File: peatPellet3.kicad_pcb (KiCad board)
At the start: 2 copper layers, 87.6 x 55.9 mm, 63 parts, among them J1 Barrel_Jack_Switch, J2 AudioJack2, J3 AudioJack2, K1 Relay_DPDT, SW1 SW_SPDT, SW2 SW_SPDT, SW3 SW_SPDT_MSM, U1 TL072, U2 L78L05_SO8, U3 LM555xM

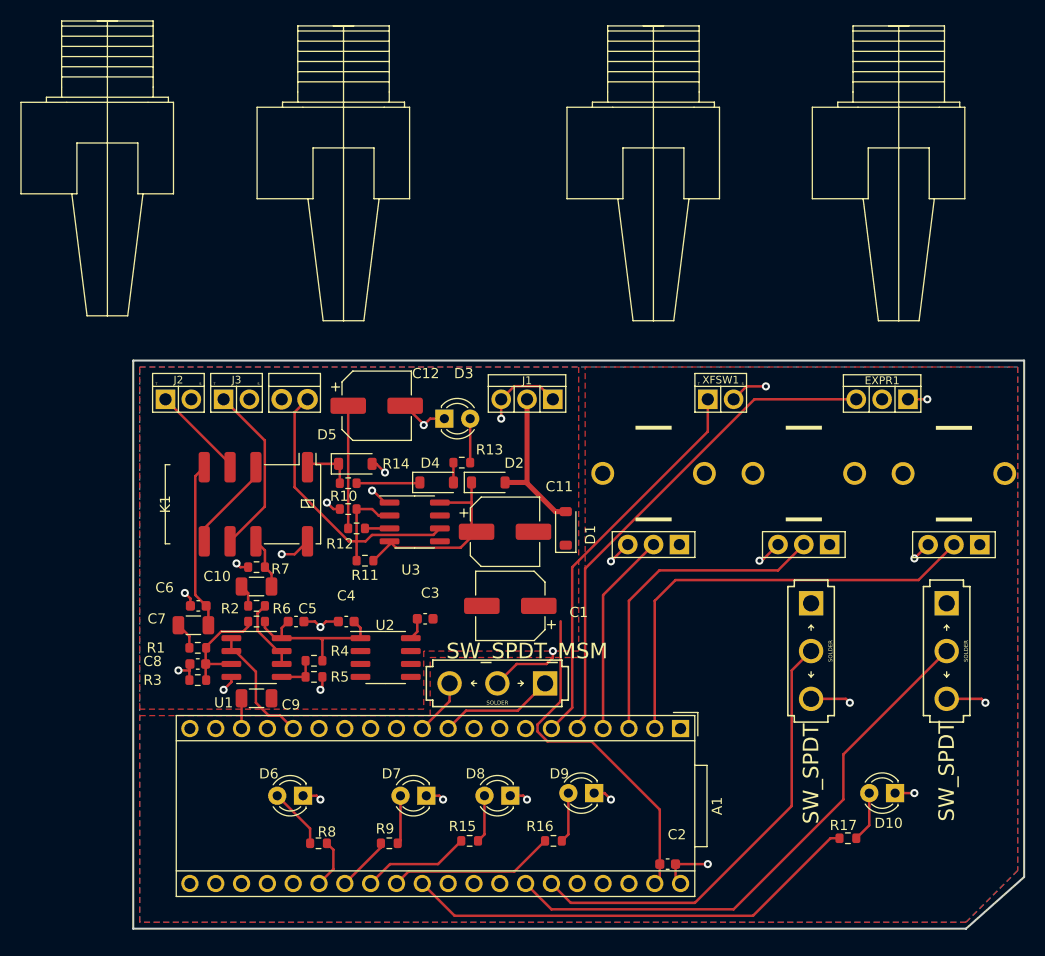
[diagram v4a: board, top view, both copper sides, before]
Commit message: power updates: grounding, 3.3v pour
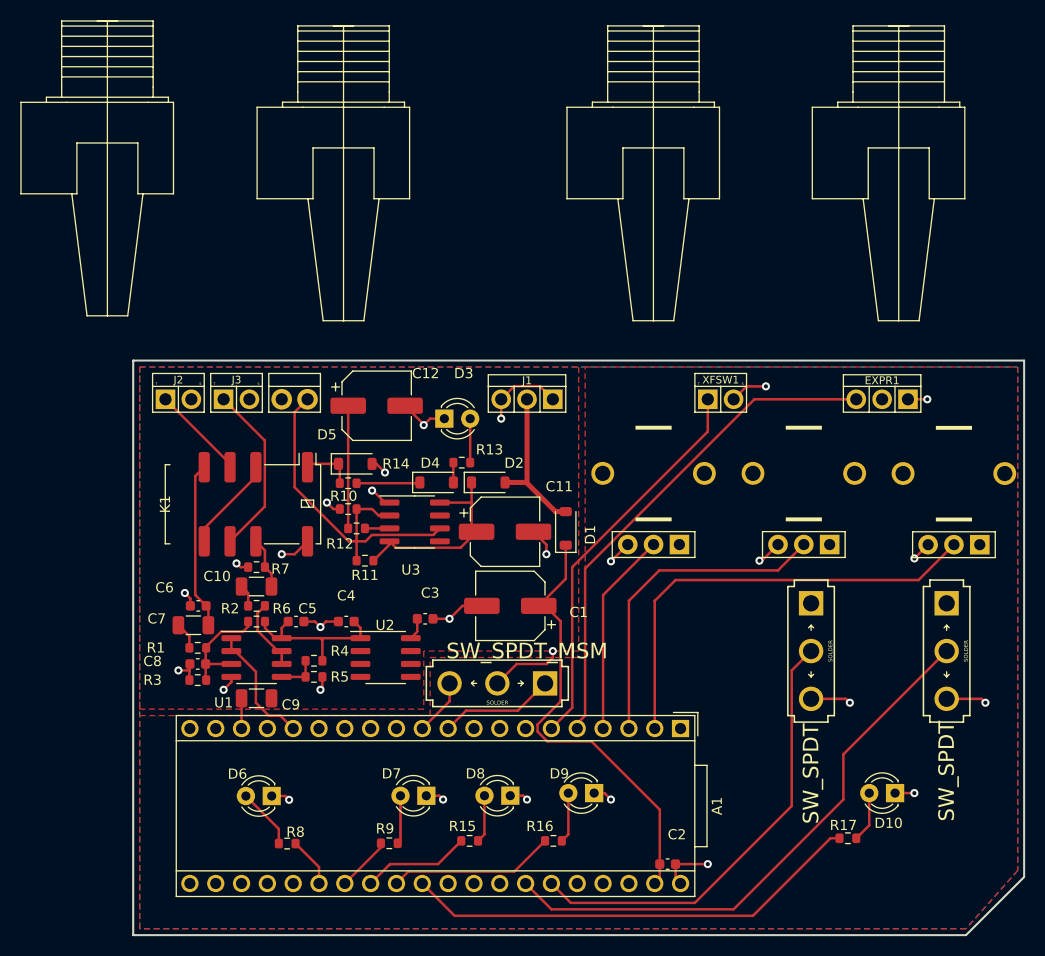
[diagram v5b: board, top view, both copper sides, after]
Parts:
- moved R8 3.08 mm to (97.7, 133.9)
- moved D6 3.08 mm to (96.2, 129.2)
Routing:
- net +9V: track 56.8 -> 66.7 mm
- net GND: track 75.8 -> 83.9 mm, vias 26 -> 28
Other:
- board size 87.6 x 55.9 mm -> 87.6 x 56.5 mm
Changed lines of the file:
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@@
   (net 68 "unconnected-(A1-ADC_3-Pad25)")
   (footprint "Resistor_SMD:R_0603_1608Metric" (layer "F.Cu")
-    (at 100.775 133.839972 180)
+    (at 97.6925 133.8675 180)
     (descr "Resistor SMD 0603 (1608 Metric), square (rectangular) end terminal, IPC_7351 nominal, (Body size source: IPC-SM-782 page 72, https://www.pcb-3d.com/wordpress/wp-content/uploads/ipc-sm-782a_amendment_1_and_2.pdf), generated with kicad-footprint-generator")
     (tags "resistor")
@@
   )
   (footprint "LED_THT:LED_D3.0mm" (layer "F.Cu")
-    (at 99.255 129.164972 180)
+    (at 96.1725 129.1925 180)
     (descr "LED, diameter 3.0mm, 2 pins")
     (tags "LED diameter 3.0mm 2 pins")
@@
     (pts
       (xy 82.55 86.36)
-      (xy 82.55 142.24)
-      (xy 164.465 142.24)
+      (xy 82.55 142.875)
+      (xy 164.465 142.875)
       (xy 170.18 137.16)
       (xy 170.18 86.36)
@@
   (segment (start 98.425 105.41) (end 97.155 105.41) (width 0.25) (layer "F.Cu") (net 17))
   (segment (start 93.075 106.68) (end 92.71 106.315) (width 0.25) (layer "F.Cu") (net 17))
+  (segment (start 114.935 110.49) (end 113.665 111.76) (width 0.25) (layer "F.Cu") (net 17))
   (segment (start 165.989 119.634) (end 166.37 120.015) (width 0.25) (layer "F.Cu") (net 17))
   (segment (start 157.485 128.905) (end 159.385 128.905) (width 0.25) (layer "F.Cu") (net 17))
   (segment (start 119.639 129.16) (end 120.904 129.16) (width 0.25) (layer "F.Cu") (net 17))
   (segment (start 101.155 118.555) (end 100.965 118.745) (width 0.25) (layer "F.Cu") (net 17))
-  (segment (start 100.589972 129.164972) (end 100.965 129.54) (width 0.25) (layer "F.Cu") (net 17))
+  (segment (start 97.507472 129.1925) (end 97.8825 129.567528) (width 0.25) (layer "F.Cu") (net 17))
   (segment (start 123.825 115.57) (end 123.825 114.935) (width 0.25) (layer "F.Cu") (net 17))
   (segment (start 111.76 92.075) (end 111.125 92.71) (width 0.25) (layer "F.Cu") (net 17))
@@
   (segment (start 135.89 137.3) (end 136.385 137.795) (width 0.25) (layer "F.Cu") (net 17))
   (segment (start 120.269 116.205) (end 123.19 116.205) (width 0.25) (layer "F.Cu") (net 17))
-  (segment (start 99.255 129.164972) (end 100.589972 129.164972) (width 0.25) (layer "F.Cu") (net 17))
+  (segment (start 96.1725 129.1925) (end 97.507472 129.1925) (width 0.25) (layer "F.Cu") (net 17))
   (segment (start 109.295 90.805) (end 111.125 92.635) (width 0.25) (layer "F.Cu") (net 17))
   (segment (start 88.175 109.765) (end 87.63 109.22) (width 0.25) (layer "F.Cu") (net 17))
+  (segment (start 121.92 103.2) (end 123.19 104.47) (width 0.25) (layer "F.Cu") (net 17))
   (segment (start 88.075 116.84) (end 88.075 116.255) (width 0.25) (layer "F.Cu") (net 17))
   (segment (start 99.695 104.14) (end 98.425 105.41) (width 0.25) (layer "F.Cu") (net 17))
@@
   (segment (start 111.379 129.164972) (end 112.653972 129.164972) (width 0.25) (layer "F.Cu") (net 17))
   (segment (start 129.54 106.1085) (end 131.191 104.4575) (width 0.25) (layer "F.Cu") (net 17))
+  (segment (start 123.19 104.47) (end 123.19 105.41) (width 0.25) (layer "F.Cu") (net 17))
   (segment (start 144.145 106.045) (end 144.3825 106.045) (width 0.25) (layer "F.Cu") (net 17))
   (segment (start 120.0352 88.8798) (end 122.5348 88.8798) (width 0.25) (layer "F.Cu") (net 17))
   (segment (start 127.889 128.905) (end 128.904 128.905) (width 0.25) (layer "F.Cu") (net 17))
+  (segment (start 116.84 110.49) (end 114.935 110.49) (width 0.25) (layer "F.Cu") (net 17))
   (segment (start 128.904 128.905) (end 129.539 129.54) (width 0.25) (layer "F.Cu") (net 17))
   (segment (start 100.4195 112.03) (end 100.965 112.5755) (width 0.25) (layer "F.Cu") (net 17))
@@
   (segment (start 141.605 90.17) (end 142.875 88.9) (width 0.25) (layer "F.Cu") (net 17))
   (segment (start 111.125 92.635) (end 111.125 92.71) (width 0.25) (layer "F.Cu") (net 17))
+  (segment (start 112.04 111.76) (end 113.665 111.76) (width 0.25) (layer "F.Cu") (net 17))
   (segment (start 99.34 112.03) (end 100.4195 112.03) (width 0.25) (layer "F.Cu") (net 17))
   (segment (start 149.225 119.634) (end 152.654 119.634) (width 0.25) (layer "F.Cu") (net 17))
@@
   (via (at 160.655 90.17) (size 0.8) (drill 0.4) (layers "F.Cu" "B.Cu") (net 17))
   (via (at 100.965 112.5755) (size 0.8) (drill 0.4) (layers "F.Cu" "B.Cu") (net 17))
-  (via (at 100.965 129.54) (size 0.8) (drill 0.4) (layers "F.Cu" "B.Cu") (net 17))
+  (via (at 97.8825 129.567528) (size 0.8) (drill 0.4) (layers "F.Cu" "B.Cu") (net 17))
   (via (at 106.045 99.1495) (size 0.8) (drill 0.4) (layers "F.Cu" "B.Cu") (net 17))
   (via (at 92.71 106.315) (size 0.8) (drill 0.4) (layers "F.Cu" "B.Cu") (net 17))
   (via (at 144.145 106.045) (size 0.8) (drill 0.4) (layers "F.Cu" "B.Cu") (net 17))
   (via (at 129.539 129.54) (size 0.8) (drill 0.4) (layers "F.Cu" "B.Cu") (net 17))
+  (via (at 123.19 105.41) (size 0.8) (drill 0.4) (layers "F.Cu" "B.Cu") (net 17))
   (via (at 97.155 105.41) (size 0.8) (drill 0.4) (layers "F.Cu" "B.Cu") (net 17))
   (via (at 111.125 92.71) (size 0.8) (drill 0.4) (layers "F.Cu" "B.Cu") (net 17))
@@
   (via (at 159.385 128.905) (size 0.8) (drill 0.4) (layers "F.Cu" "B.Cu") (net 17))
   (via (at 153.035 120.015) (size 0.8) (drill 0.4) (layers "F.Cu" "B.Cu") (net 17))
+  (via (at 113.665 111.76) (size 0.8) (drill 0.4) (layers "F.Cu" "B.Cu") (net 17))
   (via (at 129.54 106.1085) (size 0.8) (drill 0.4) (layers "F.Cu" "B.Cu") (net 17))
   (via (at 166.37 120.015) (size 0.8) (drill 0.4) (layers "F.Cu" "B.Cu") (net 17))
@@
   (segment (start 143.653881 90.17) (end 153.67 90.17) (width 0.25) (layer "F.Cu") (net 22))
   (segment (start 127 106.823881) (end 143.653881 90.17) (width 0.25) (layer "F.Cu") (net 22))
-  (segment (start 102.235 134.474972) (end 102.235 136.385) (width 0.25) (layer "F.Cu") (net 23))
-  (segment (start 102.235 136.385) (end 100.825 137.795) (width 0.25) (layer "F.Cu") (net 23))
-  (segment (start 101.6 133.839972) (end 102.235 134.474972) (width 0.25) (layer "F.Cu") (net 23))
+  (segment (start 100.825 136.175) (end 98.5175 133.8675) (width 0.25) (layer "F.Cu") (net 23))
+  (segment (start 100.825 137.795) (end 100.825 136.175) (width 0.25) (layer "F.Cu") (net 23))
   (segment (start 106.914 133.839972) (end 106.914 134.246) (width 0.25) (layer "F.Cu") (net 24))
   (segment (start 106.914 134.246) (end 103.365 137.795) (width 0.25) (layer "F.Cu") (net 24))
@@
   (segment (start 103.695 102.87) (end 103.695 90.805) (width 0.25) (layer "F.Cu") (net 54))
   (segment (start 115.695 92.075) (end 115.695 96.52) (width 0.25) (layer "F.Cu") (net 55))
-  (segment (start 99.95 132.399972) (end 99.95 133.839972) (width 0.25) (layer "F.Cu") (net 56))
-  (segment (start 96.715 129.164972) (end 99.95 132.399972) (width 0.25) (layer "F.Cu") (net 56))
+  (segment (start 96.8675 132.4275) (end 96.8675 133.8675) (width 0.25) (layer "F.Cu") (net 56))
+  (segment (start 93.6325 129.1925) (end 96.8675 132.4275) (width 0.25) (layer "F.Cu") (net 56))
   (segment (start 108.839 133.564972) (end 108.564 133.839972) (width 0.25) (layer "F.Cu") (net 57))
   (segment (start 108.839 129.164972) (end 108.839 133.564972) (width 0.25) (layer "F.Cu") (net 57))
@@
   (segment (start 107.76 104.455) (end 107.76 104.14) (width 0.25) (layer "F.Cu") (net 66))
   (segment (start 112.71 100.33) (end 115.825 100.33) (width 0.25) (layer "F.Cu") (net 66))
+  (segment (start 125.095 104.52) (end 125.095 107.835) (width 0.25) (layer "F.Cu") (net 66))
   (segment (start 124.588 119.887) (end 122.32 122.155) (width 0.25) (layer "F.Cu") (net 66))
   (segment (start 110.49 113.03) (end 109.855 113.665) (width 0.25) (layer "F.Cu") (net 66))
+  (segment (start 122.44 110.49) (end 123.075 110.49) (width 0.25) (layer "F.Cu") (net 66))
   (segment (start 108.385 104.765) (end 114.755 104.765) (width 0.25) (layer "F.Cu") (net 66))
   (segment (start 134.34 130.53) (end 127.635 123.825) (width 0.25) (layer "F.Cu") (net 66))
@@
   (segment (start 115.825 98.35) (end 115.825 100.33) (width 0.25) (layer "F.Cu") (net 66))
   (segment (start 110.49 111.76) (end 110.49 113.03) (width 0.25) (layer "F.Cu") (net 66))
+  (segment (start 125.095 107.835) (end 122.44 110.49) (width 0.25) (layer "F.Cu") (net 66))
   (segment (start 115.825 102.705) (end 116.32 103.2) (width 0.25) (layer "F.Cu") (net 66))
   (segment (start 115.825 100.33) (end 115.825 102.705) (width 0.25) (layer "F.Cu") (net 66))
@@
   (segment (start 123.293299 123.825) (end 127.635 123.825) (width 0.25) (layer "F.Cu") (net 66))
   (segment (start 134.34 135.89) (end 134.34 137.3) (width 0.25) (layer "F.Cu") (net 66))
+  (segment (start 123.075 110.49) (end 124.588 112.003) (width 0.25) (layer "F.Cu") (net 66))
   (zone (net 66) (net_name "+9V") (layer "F.Cu") (hatch edge 0.5)
     (priority 1)
@@
         (xy 169.545 86.995)
         (xy 169.545 136.525)
-        (xy 164.465 141.605)
-        (xy 83.185 141.605)
+        (xy 164.465 142.24)
+        (xy 83.185 142.24)
         (xy 83.185 121.285)
         (xy 111.76 121.285)
@@
         (xy 169.545 86.995)
         (xy 169.545 136.525)
-        (xy 164.465 141.605)
-        (xy 83.185 141.605)
+        (xy 164.465 142.24)
+        (xy 83.185 142.24)
       )
     )

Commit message: via updates
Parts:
- D10, D6, D7, D8, D9: moved to B.Cu
- moved D9 3.06 mm to (124.8, 129.2), turned to 0 degrees
- moved D8 2.80 mm to (116.8, 129.2), turned to 0 degrees
- moved D10 2.55 mm to (154.9, 128.9), turned to 0 degrees
- moved D7 2.54 mm to (108.8, 129.2), turned to 0 degrees
- moved D6 1.85 mm to (94.3, 129.2), turned to 0 degrees
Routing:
- net GND: track 83.9 -> 50.1 mm, vias 28 -> 12
- net Net-(U1B-+): track 3.94 -> 6.46 mm
- net Net-(D10-A): track 4.97 -> 6.39 mm
- net Net-(D6-A): track 6.01 -> 4.70 mm
- net Net-(D7-A): track 4.79 -> 5.84 mm
- net Net-(D8-A): track 4.71 -> 5.72 mm
- net Net-(D9-A): track 4.97 -> 5.63 mm

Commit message: LED flips
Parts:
- D3: moved to B.Cu
- moved D3 0.13 mm to (113.0, 92.1)
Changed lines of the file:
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@@
     )
   )
-  (footprint "LED_THT:LED_D3.0mm" (layer "F.Cu")
-    (at 113.155 92.075)
-    (descr "LED, diameter 3.0mm, 2 pins")
-    (tags "LED diameter 3.0mm 2 pins")
-    (property "Sheetfile" "peatPellet3.kicad_sch")
-    (property "Sheetname" "")
-    (property "ki_description" "Light emitting diode")
-    (property "ki_keywords" "LED diode")
-    (attr through_hole)
-    (fp_text reference "D3" (at 1.905 -4.445) (layer "F.SilkS")
-        (effects (font (size 1 1) (thickness 0.15)))
-    )
-    (fp_text value "LED" (at 1.905 -3.175) (layer "F.Fab")
-        (effects (font (size 1 1) (thickness 0.15)))
-    )
-    (fp_line (start -0.29 -1.236) (end -0.29 -1.08)
-      (stroke (width 0.12) (type solid)) (layer "F.SilkS"))
-    (fp_line (start -0.29 1.08) (end -0.29 1.236)
-      (stroke (width 0.12) (type solid)) (layer "F.SilkS"))
-    (fp_arc (start -0.29 -1.235516) (mid 1.366487 -1.987659) (end 2.942335 -1.078608)
-      (stroke (width 0.12) (type solid)) (layer "F.SilkS"))
-    (fp_arc (start 0.229039 -1.08) (mid 1.270117 -1.5) (end 2.31113 -1.079837)
-      (stroke (width 0.12) (type solid)) (layer "F.SilkS"))
-    (fp_arc (start 2.31113 1.079837) (mid 1.270117 1.5) (end 0.229039 1.08)
-      (stroke (width 0.12) (type solid)) (layer "F.SilkS"))
-    (fp_arc (start 2.942335 1.078608) (mid 1.366487 1.987659) (end -0.29 1.235516)
-      (stroke (width 0.12) (type solid)) (layer "F.SilkS"))
-    (fp_line (start -1.15 -2.25) (end -1.15 2.25)
-      (stroke (width 0.05) (type solid)) (layer "F.CrtYd"))
-    (fp_line (start -1.15 2.25) (end 3.7 2.25)
-      (stroke (width 0.05) (type solid)) (layer "F.CrtYd"))
-    (fp_line (start 3.7 -2.25) (end -1.15 -2.25)
-      (stroke (width 0.05) (type solid)) (layer "F.CrtYd"))
-    (fp_line (start 3.7 2.25) (end 3.7 -2.25)
-      (stroke (width 0.05) (type solid)) (layer "F.CrtYd"))
-    (fp_line (start -0.23 -1.16619) (end -0.23 1.16619)
-      (stroke (width 0.1) (type solid)) (layer "F.Fab"))
-    (fp_arc (start -0.23 -1.16619) (mid 3.17 0.000452) (end -0.230555 1.165476)
-      (stroke (width 0.1) (type solid)) (layer "F.Fab"))
-    (fp_circle (center 1.27 0) (end 2.77 0)
-      (stroke (width 0.1) (type solid)) (fill none) (layer "F.Fab"))
-    (pad "1" thru_hole rect (at 0 0) (size 1.8 1.8) (drill 0.9) (layers "*.Cu" "*.Mask")
-      (net 17 "GND") (pinfunction "K") (pintype "passive"))
-    (pad "2" thru_hole circle (at 2.54 0) (size 1.8 1.8) (drill 0.9) (layers "*.Cu" "*.Mask")
-      (net 55 "Net-(D3-A)") (pinfunction "A") (pintype "passive"))
-    (model "${KICAD6_3DMODEL_DIR}/LED_THT.3dshapes/LED_D3.0mm.wrl"
-      (offset (xyz 0 0 0))
-      (scale (xyz 1 1 1))
-      (rotate (xyz 0 0 0))
-    )
-  )
   (footprint "Package_SO:SOIC-8_3.9x4.9mm_P1.27mm" (layer "F.Cu")
     (at 110.235 102.235)
@@
     )
   )
+  (footprint "LED_THT:LED_D3.0mm" (layer "B.Cu")
+    (at 113.025 92.075)
+    (descr "LED, diameter 3.0mm, 2 pins")
+    (tags "LED diameter 3.0mm 2 pins")
+    (property "Sheetfile" "peatPellet3.kicad_sch")
+    (property "Sheetname" "")
+    (property "ki_description" "Light emitting diode")
+    (property "ki_keywords" "LED diode")
+    (attr through_hole)
+    (fp_text reference "D3" (at 1.27 -3.175 -360) (layer "B.SilkS")
+        (effects (font (size 1 1) (thickness 0.15)) (justify mirror))
+    )
+    (fp_text value "LED" (at 1.27 -4.445 -360) (layer "B.Fab")
+        (effects (font (size 1 1) (thickness 0.15)) (justify mirror))
+    )
+    (fp_line (start -0.29 -1.08) (end -0.29 -1.236)
+      (stroke (width 0.12) (type solid)) (layer "B.SilkS"))
+    (fp_line (start -0.29 1.236) (end -0.29 1.08)
+      (stroke (width 0.12) (type solid)) (layer "B.SilkS"))
+    (fp_arc (start -0.29 -1.235516) (mid 1.366487 -1.987659) (end 2.942335 -1.078608)
+      (stroke (width 0.12) (type solid)) (layer "B.SilkS"))
+    (fp_arc (start 0.229039 -1.08) (mid 1.270117 -1.5) (end 2.31113 -1.079837)
+      (stroke (width 0.12) (type solid)) (layer "B.SilkS"))
+    (fp_arc (start 2.31113 1.079837) (mid 1.270117 1.5) (end 0.229039 1.08)
+      (stroke (width 0.12) (type solid)) (layer "B.SilkS"))
+    (fp_arc (start 2.942335 1.078608) (mid 1.366487 1.987659) (end -0.29 1.235516)
+      (stroke (width 0.12) (type solid)) (layer "B.SilkS"))
+    (fp_line (start -1.15 -2.25) (end 3.7 -2.25)
+      (stroke (width 0.05) (type solid)) (layer "B.CrtYd"))
+    (fp_line (start -1.15 2.25) (end -1.15 -2.25)
+      (stroke (width 0.05) (type solid)) (layer "B.CrtYd"))
+    (fp_line (start 3.7 -2.25) (end 3.7 2.25)
+      (stroke (width 0.05) (type solid)) (layer "B.CrtYd"))
+    (fp_line (start 3.7 2.25) (end -1.15 2.25)
+      (stroke (width 0.05) (type solid)) (layer "B.CrtYd"))
+    (fp_line (start -0.23 1.16619) (end -0.23 -1.16619)
+      (stroke (width 0.1) (type solid)) (layer "B.Fab"))
+    (fp_arc (start -0.230555 -1.165476) (mid 3.17 -0.000452) (end -0.23 1.16619)
+      (stroke (width 0.1) (type solid)) (layer "B.Fab"))
+    (fp_circle (center 1.27 0) (end 2.77 0)
+      (stroke (width 0.1) (type solid)) (fill none) (layer "B.Fab"))
+    (pad "1" thru_hole rect (at 0 0) (size 1.8 1.8) (drill 0.9) (layers "*.Cu" "*.Mask")
+      (net 17 "GND") (pinfunction "K") (pintype "passive"))
+    (pad "2" thru_hole circle (at 2.54 0) (size 1.8 1.8) (drill 0.9) (layers "*.Cu" "*.Mask")
+      (net 55 "Net-(D3-A)") (pinfunction "A") (pintype "passive"))
+    (model "${KICAD6_3DMODEL_DIR}/LED_THT.3dshapes/LED_D3.0mm.wrl"
+      (offset (xyz 0 0 0))
+      (scale (xyz 1 1 1))
+      (rotate (xyz 0 0 0))
+    )
+  )
   (footprint "jacks:3PADS" (layer "B.Cu")
     (at 156.21 90.17 180)
@@
   (segment (start 102.73 112.03) (end 101.5105 112.03) (width 0.25) (layer "F.Cu") (net 17))
   (segment (start 103.53 111.23) (end 102.73 112.03) (width 0.25) (layer "F.Cu") (net 17))
+  (segment (start 113.025 92.075) (end 110.565 92.075) (width 0.25) (layer "F.Cu") (net 17))
   (segment (start 106.045 96.52) (end 106.4645 96.52) (width 0.25) (layer "F.Cu") (net 17))
   (segment (start 110.231751 114.935) (end 112.04 113.126751) (width 0.25) (layer "F.Cu") (net 17))
+  (segment (start 110.565 92.075) (end 109.295 90.805) (width 0.25) (layer "F.Cu") (net 17))
   (segment (start 98.425 105.41) (end 97.155 105.41) (width 0.25) (layer "F.Cu") (net 17))
-  (segment (start 110.565 92.075) (end 113.155 92.075) (width 0.25) (layer "F.Cu") (net 17))
   (segment (start 93.075 106.68) (end 92.71 106.315) (width 0.25) (layer "F.Cu") (net 17))
   (segment (start 114.935 110.49) (end 113.665 111.76) (width 0.25) (layer "F.Cu") (net 17))
@@
   (segment (start 116.84 110.49) (end 114.935 110.49) (width 0.25) (layer "F.Cu") (net 17))
   (segment (start 104.88 111.23) (end 103.53 111.23) (width 0.25) (layer "F.Cu") (net 17))
-  (segment (start 109.295 90.805) (end 110.565 92.075) (width 0.25) (layer "F.Cu") (net 17))
   (segment (start 100.4195 112.03) (end 100.965 112.5755) (width 0.25) (layer "F.Cu") (net 17))
   (segment (start 107.76 100.33) (end 107.315 100.33) (width 0.25) (layer "F.Cu") (net 17))
@@
   (segment (start 93.855 109.235) (end 93.205 108.585) (width 0.25) (layer "F.Cu") (net 53))
   (segment (start 103.695 102.87) (end 103.695 90.805) (width 0.25) (layer "F.Cu") (net 54))
-  (segment (start 115.695 92.075) (end 115.695 96.52) (width 0.25) (layer "F.Cu") (net 55))
+  (segment (start 115.695 96.4) (end 115.565 96.27) (width 0.25) (layer "F.Cu") (net 55))
+  (segment (start 115.565 96.27) (end 115.565 92.075) (width 0.25) (layer "F.Cu") (net 55))
   (segment (start 96.8675 133.8675) (end 96.8675 129.164972) (width 0.25) (layer "F.Cu") (net 56))
   (segment (start 108.564 133.839972) (end 111.3775 131.026472) (width 0.25) (layer "F.Cu") (net 57))
